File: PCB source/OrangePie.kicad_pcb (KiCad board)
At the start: 2 copper layers, 100 x 100 mm, 143 parts, among them J1 09031967921, J2 Orange pi 5 pro, J3 JST XH, J5 Connector, USB-TYPE-C-16P, M1 Fan, Q1 AO3400A, Q2 AO3400A, Q4 AO3400A, Q5 MMBT3904, U1 IP4234CZ6,115, U10 CH334R, U11 CH340G, U12 IP4234CZ6, U13 AMS1117-3.3, U2 SIC431AED-T1-GE3, U3 STM32G431C8Tx, U4 LM74700, U5 LM74700, U6 TJA1044GTK_3Z, U7 TJA1044GTK_3Z, U8 TDA7052A, U9 PCM2704CDBR, X1 X322512MSB4SI, Y1 12MHz, Y2 12MHz C7424717

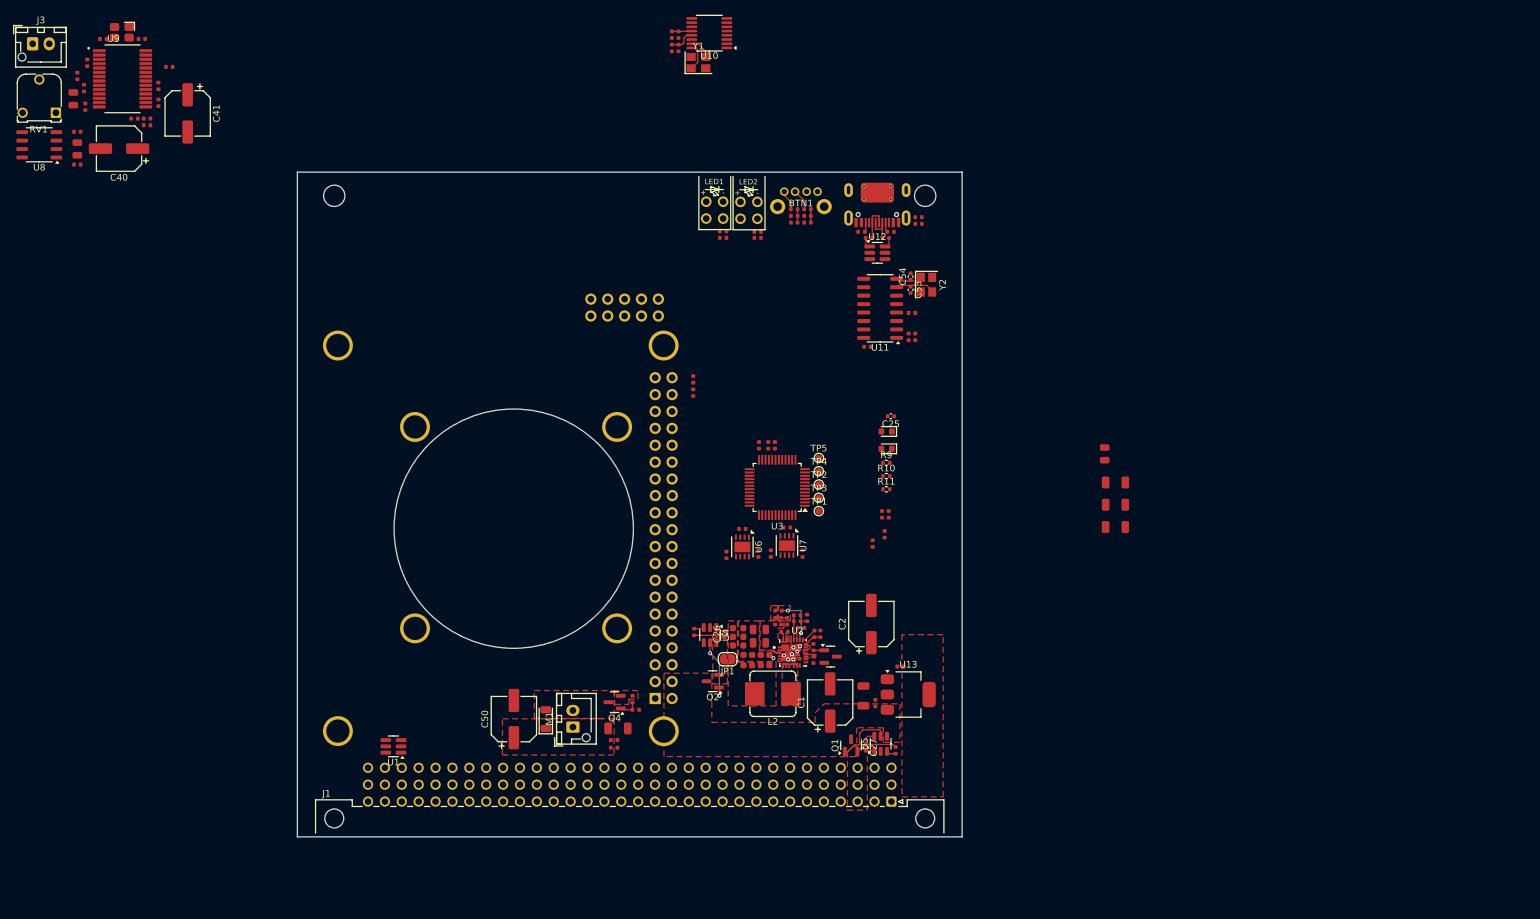
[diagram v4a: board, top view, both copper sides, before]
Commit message: Create v1 floorplan
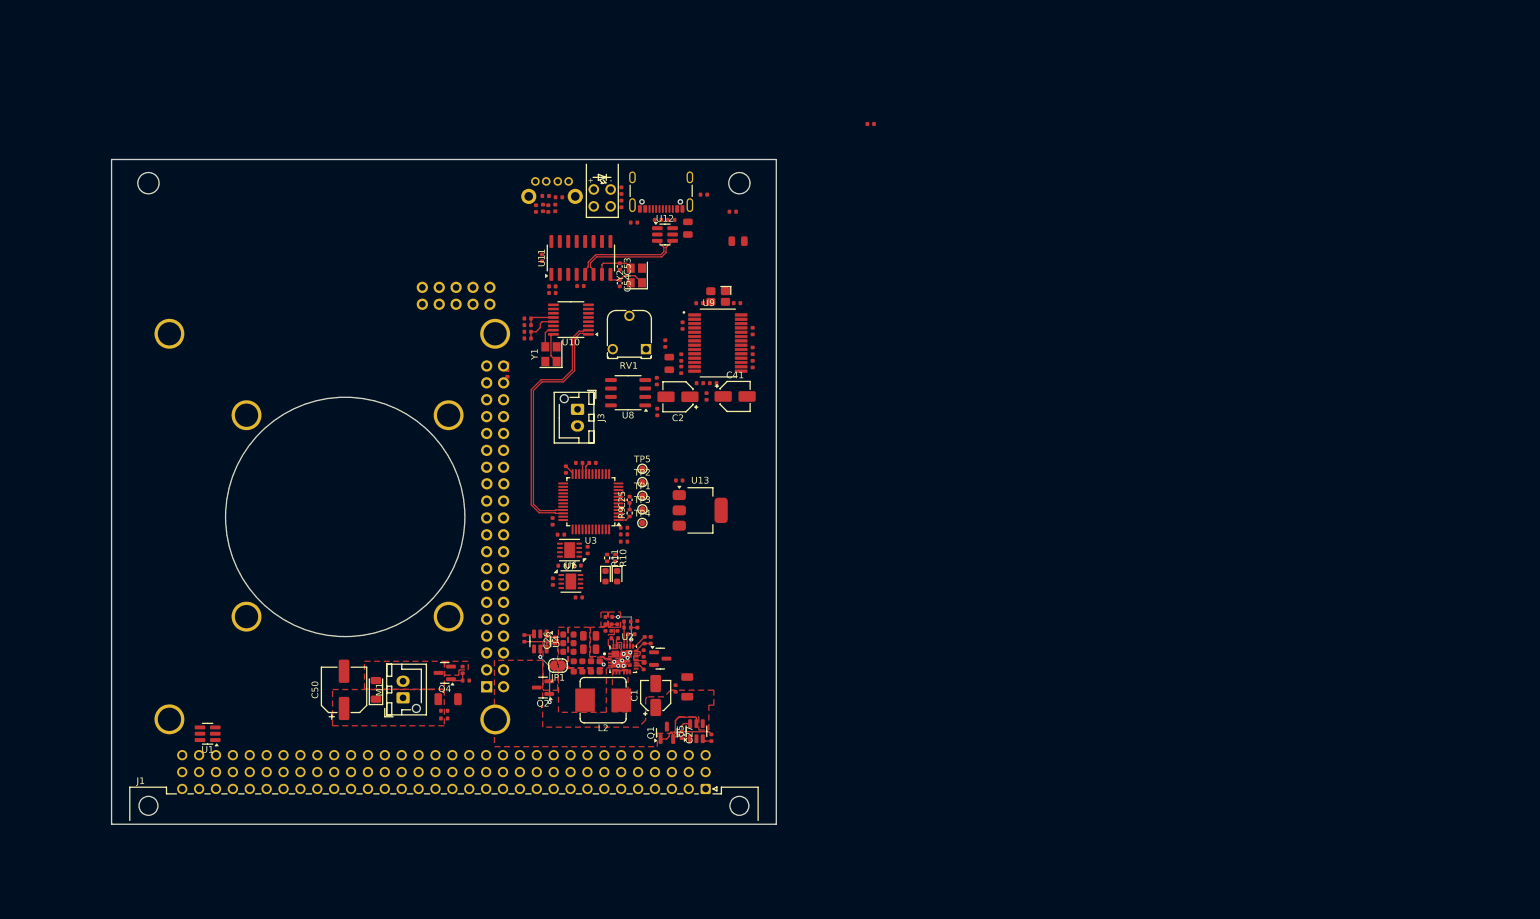
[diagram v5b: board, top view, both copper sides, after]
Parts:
- removed C3, C4, C5: 10uF, PCM_JLCPCB:C_1206
- removed C40: 47uF, Capacitor_SMD:CP_Elec_6.3x5.4
- removed D2: Green, PCM_JLCPCB:D_0603
- removed LED2: FixLed307, FixLed307:FixLed307
- removed R34, R35: 1kΩ, PCM_JLCPCB:R_0402
- added D1: Yellow, PCM_JLCPCB:D_0603, F.Cu at (106.8, 101.2)
- C1, C2, C41: footprint Capacitor_SMD:CP_Elec_6.3x5.4 -> Capacitor_SMD:CP_Elec_4x5.4
- J5: footprint PCM_JLCPCB:TYPE-C-SMD_HX-TYPE-C-16PIN -> Connector_USB:USB_C_Receptacle_GCT_USB4105-xx-A_16P_TopMnt_Horizontal
- moved C33 100.4 mm to (125.0, 50.8), turned to 0 degrees
- moved J3 98.7 mm to (100.8, 76.1), turned to -90 degrees
- moved C32 98.6 mm to (116.4, 68.3), turned to -90 degrees
- moved C44 98.1 mm to (119.2, 60.1)
- moved X1 98.1 mm to (122.0, 59.1)
- moved C37 98.1 mm to (114.6, 69.2)
- moved C35 98.0 mm to (116.4, 70.2)
- moved U9 98.0 mm to (121.9, 66.1)
- moved C43 98.0 mm to (124.8, 60.1)
- moved R22 97.9 mm to (116.6, 63.5)
- moved C39 97.9 mm to (127.2, 67.3)
- moved C38 97.7 mm to (127.2, 69.3)
- moved R19 97.2 mm to (114.0, 66.2)
- moved C34 96.4 mm to (127.2, 64.3), turned to -90 degrees
- moved U8 96.1 mm to (108.4, 73.6)
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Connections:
- net /USB-CAN/LED_TX renamed /USB-CAN/WORD_LED
- C2 pad 1: +5V -> Net-(C2-Pad1)
- C2 pad 2: GND -> Net-(U8-+)
- LED1 pad 3: +3V3 -> +5V
- R10 pad 1: /USB-CAN/LED_RX -> /USB-CAN/STAT_LED
- R16 pad 2: Net-(C40-Pad1) -> Net-(C2-Pad1)
- R17 pad 2: Net-(C40-Pad1) -> Net-(C2-Pad1)
- R18 pad 2: Net-(C40-Pad1) -> Net-(C2-Pad1)
- U3 pad 39: unconnected-(U3-PA15-Pad39) -> /USB-CAN/STAT_LED
- U3 pad 9: /USB-CAN/LED_RX -> unconnected-(U3-PA1-Pad9)
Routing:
- net /USB HUB/USB_CAN.D+: track 0.00 -> 37.8 mm
- net /USB HUB/USB_CAN.D-: track 0.00 -> 36.7 mm
- net /CH340_DEBUG/FRONT_PANEL.D-: track 0.00 -> 16.1 mm
- net /CH340_DEBUG/FRONT_PANEL.D+: track 0.00 -> 16.1 mm
- net +3V3: track 0.00 -> 7.04 mm
- net Net-(J5-D--PadA7): track 5.26 -> 0.00 mm
- net Net-(J5-D+-PadA6): track 5.26 -> 0.00 mm
- net Net-(BTN1-Pad3): track 3.22 -> 0.00 mm
- net Net-(BTN1-Pad4): track 3.13 -> 0.00 mm
- net /USB-CAN/NRST1: track 0.00 -> 2.86 mm
- net Net-(U11-XO): track 4.02 -> 6.24 mm
- net /OrangePi 5 pro Header/USER BUTTON: track 2.00 -> 0.00 mm
- net /OrangePi 5 pro Header/ON OFF BTN: track 2.00 -> 0.00 mm
- net /Panel USB/USB_IN.D+: track 1.89 -> 0.00 mm
- net /Panel USB/USB_IN.D-: track 1.89 -> 0.00 mm
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- removed copper zone on F.Cu, net +3V3
- removed copper zone on F.Cu, net /DIN41612 connector/5v_STDBY
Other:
- outline, holes or cut-outs redrawn
- copper layers 2 -> 4
- board text added: "0"
- board text added: "0 mm"
- board text added: "0.01 mm"
- board text added: "0.0152 mm"
- board text added: "0.02"
- board text added: "0.035 mm"
- board text added: "0.2104 mm"
- board text added: "1"
- board text added: "1.065 mm"
- board text added: "3.3"
- board text added: "4.4"
- board text added: "4.6"
- board text added: "B.Cu"
- board text added: "B.Mask"
- board text added: "B.Paste"
- board text added: "B.Silkscreen"
- board text added: "Black"
- board text added: "Bottom Silk Screen"
- board text added: "Bottom Solder Mask"
- board text added: "Bottom Solder Paste"
- board text added: "Color"
- board text added: "Dielectric 1"
- board text added: "Dielectric 2"
- board text added: "Dielectric 3"
- board text added: "Epsilon R"
- board text added: "F.Cu"
- board text added: "F.Mask"
- board text added: "F.Paste"
- board text added: "F.Silkscreen"
- board text added: "FR4"
- board text added: "FR4 natural"
- board text added: "In1.Cu"
- board text added: "In2.Cu"
- board text added: "Layer Name"
- board text added: "Loss Tangent"
- board text added: "Material"
- board text added: "Not specified"
- board text added: "Thickness (mm)"
- board text added: "Top Silk Screen"
- board text added: "Top Solder Mask"
- board text added: "Top Solder Paste"
- board text added: "Type"
- board text added: "White"
- board text added: "copper"
- board text added: "core"
- board text added: "prepreg"
